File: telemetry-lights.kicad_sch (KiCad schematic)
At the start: 23 parts, among them J1 Conn_01x02, J2 Conn_01x04, J6 Conn_01x02, J8 Conn_01x02, Q1 AO3400A, U1 STM32L431KBU6TR, U2 INA228, U3 IAM-20381HT

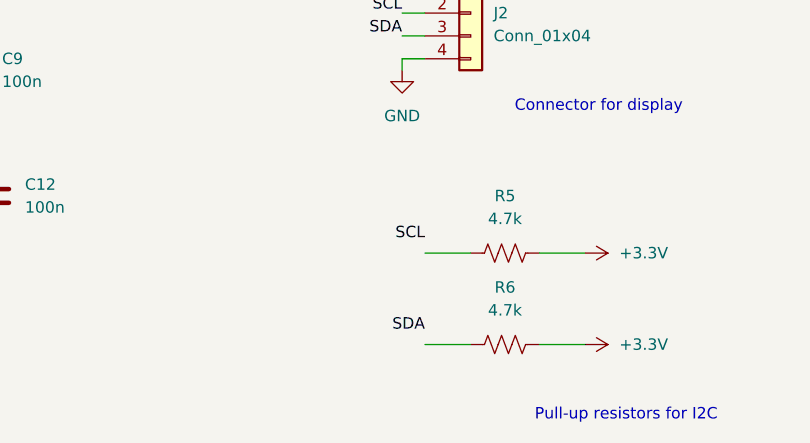
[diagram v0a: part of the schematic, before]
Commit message: added footprints
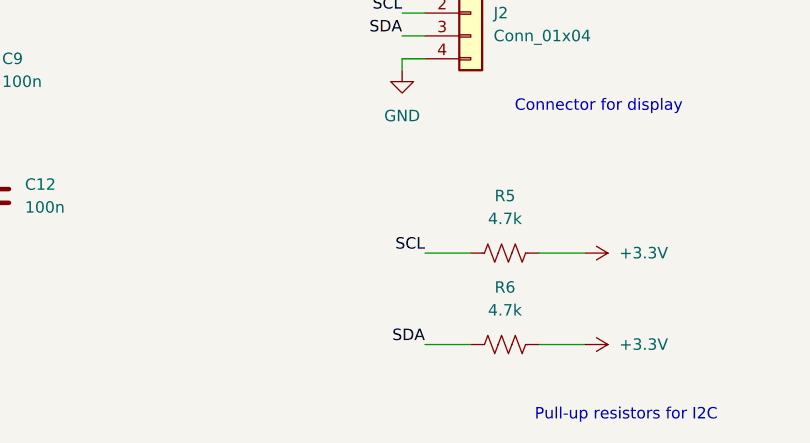
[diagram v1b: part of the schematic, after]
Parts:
- C1, C2, C3, C4, C5: footprint (none) -> Capacitor_SMD:C_0805_2012Metric_Pad1.18x1.45mm_HandSolder
- J1: footprint (none) -> Connector_JST:JST_PH_B2B-PH-K_1x02_P2.00mm_Vertical
- J2: footprint (none) -> Connector_JST:JST_PH_B4B-PH-K_1x04_P2.00mm_Vertical
- R1: footprint (none) -> Resistor_SMD:R_Shunt_Ohmite_LVK20
- R2, R3, R5, R6: footprint (none) -> Resistor_SMD:R_0805_2012Metric_Pad1.20x1.40mm_HandSolder
- U1: footprint UFQFPN-32 -> telemetry-lights:UFQFPN-32
- U2: footprint Package_SO:VSSOP-10_3x3mm_P0.5mm -> telemetry-lights:VSSOP-10_3x3mm_P0.5mm
- U3: footprint IAM-20381HT:XDCR_IAM-20381HT -> telemetry-lights:XDCR_IAM-20381HT
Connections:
- net SCL: now also R5.1
- net SDA: now also R6.1
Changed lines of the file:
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@@
 	)
 	(label "SDA"
-		(at 123.19 177.8 180)
+		(at 123.19 179.07 180)
 		(effects
 			(font
@@
 	)
 	(label "SCL"
-		(at 123.19 167.64 180)
+		(at 123.19 168.91 180)
 		(effects
 			(font
@@
 			)
 		)
-		(property "Footprint" "UFQFPN-32"
+		(property "Footprint" "telemetry-lights:UFQFPN-32"
 			(at 34.29 90.17 0)
 			(hide yes)
@@
 			)
 		)
-		(property "Footprint" "Package_SO:VSSOP-10_3x3mm_P0.5mm"
+		(property "Footprint" "telemetry-lights:VSSOP-10_3x3mm_P0.5mm"
 			(at 193.04 62.23 0)
 			(hide yes)
@@
 			)
 		)
-		(property "Footprint" ""
+		(property "Footprint" "Capacitor_SMD:C_0805_2012Metric_Pad1.18x1.45mm_HandSolder"
 			(at 106.68 98.0948 0)
 			(hide yes)
@@
 			)
 		)
-		(property "Footprint" ""
+		(property "Footprint" "Capacitor_SMD:C_0805_2012Metric_Pad1.18x1.45mm_HandSolder"
 			(at 106.68 105.7148 0)
 			(hide yes)
@@
 			)
 		)
-		(property "Footprint" ""
+		(property "Footprint" "Resistor_SMD:R_Shunt_Ohmite_LVK20"
 			(at 151.892 54.61 90)
 			(hide yes)
@@
 			)
 		)
-		(property "Footprint" ""
+		(property "Footprint" "Resistor_SMD:R_0805_2012Metric_Pad1.20x1.40mm_HandSolder"
 			(at 101.854 61.214 90)
 			(hide yes)
@@
 			)
 		)
-		(property "Footprint" ""
+		(property "Footprint" "Resistor_SMD:R_0805_2012Metric_Pad1.20x1.40mm_HandSolder"
 			(at 101.854 66.294 90)
 			(hide yes)
@@
 			)
 		)
-		(property "Footprint" ""
+		(property "Footprint" "Resistor_SMD:R_0805_2012Metric_Pad1.20x1.40mm_HandSolder"
 			(at 132.334 167.894 90)
 			(hide yes)
@@
 			)
 		)
-		(property "Footprint" ""
+		(property "Footprint" "Connector_JST:JST_PH_B4B-PH-K_1x04_P2.00mm_Vertical"
 			(at 128.27 142.24 0)
 			(hide yes)
@@
 			)
 		)
-		(property "Footprint" "IAM-20381HT:XDCR_IAM-20381HT"
+		(property "Footprint" "telemetry-lights:XDCR_IAM-20381HT"
 			(at 241.3 60.96 0)
 			(hide yes)
@@
 			)
 		)
-		(property "Footprint" "UFQFPN-32"
+		(property "Footprint" "telemetry-lights:UFQFPN-32"
 			(at 24.13 34.29 0)
 			(hide yes)
@@
 			)
 		)
-		(property "Footprint" ""
+		(property "Footprint" "Capacitor_SMD:C_0805_2012Metric_Pad1.18x1.45mm_HandSolder"
 			(at 105.41 79.0448 0)
 			(hide yes)
@@
 			)
 		)
-		(property "Footprint" ""
+		(property "Footprint" "Connector_JST:JST_PH_B2B-PH-K_1x02_P2.00mm_Vertical"
 			(at 176.53 77.47 0)
 			(hide yes)
@@
 			)
 		)
-		(property "Footprint" ""
+		(property "Footprint" "Capacitor_SMD:C_0805_2012Metric_Pad1.18x1.45mm_HandSolder"
 			(at 266.7 56.8452 0)
 			(hide yes)
@@
 			)
 		)
-		(property "Footprint" ""
+		(property "Footprint" "Capacitor_SMD:C_0805_2012Metric_Pad1.18x1.45mm_HandSolder"
 			(at 86.0552 110.49 0)
 			(hide yes)
@@
 			)
 		)
-		(property "Footprint" ""
+		(property "Footprint" "Resistor_SMD:R_0805_2012Metric_Pad1.20x1.40mm_HandSolder"
 			(at 132.334 178.054 90)
 			(hide yes)

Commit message: Updated input connectors and fixed ground and source orientation
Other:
- moved on the sheet: C11, C12, C8, C9, J8
